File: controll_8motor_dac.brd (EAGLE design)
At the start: 101.6 x 73.3 mm, 60 parts

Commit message: version1 できた． なかなか配線がやばいものだなぁ．
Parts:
- DC-JACK: device con-jack:SPC4077 -> BD6211F:SPC4077
- moved DC-JACK 81.3 mm to (14.0, 20.3)
- moved C1 27.0 mm to (80.0, 49.5), turned to 90 degrees
- moved LTC1660_2 16.3 mm to (62.2, 47.0), turned to 180 degrees
- moved LTC1660_1 10.2 mm to (29.2, 48.3)
- moved CHIPSELECT 7.62 mm to (87.6, 22.9)
- moved MCP3208‐1 7.62 mm to (45.7, 27.9)
- moved ARDUINO11~1 7.62 mm to (92.7, 31.8)
- moved ARDUINO11~13 7.62 mm to (87.6, 31.8)
- moved ARDUINO-5V/GND 5.08 mm to (92.7, 48.3)
- moved C2 3.59 mm to (7.62, 48.3)
- moved 安定化電源1 2.54 mm to (92.7, 57.1)
- moved ARDUINO5V/GND 2.54 mm to (90.2, 48.3)
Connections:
- new net N$26: LTC1660_1.14, M-DRIVER_3.5
- net N$3: no longer LTC1660_1.14, M-DRIVER_3.5
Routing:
- net P-DIORD1: track 0.00 -> 536.0 mm
- net N$97: track 0.00 -> 207.2 mm
- net N$33: track 0.00 -> 196.1 mm
- net ARDUINO-5V/GND: track 0.00 -> 193.9 mm
- net N$39: track 0.00 -> 100.8 mm
- net N$25: track 0.00 -> 90.9 mm
- net N$38: track 0.00 -> 85.5 mm
- net N$59: track 0.00 -> 76.2 mm
- net N$41: track 0.00 -> 69.3 mm
- net N$5: track 0.00 -> 60.1 mm
- net N$42: track 0.00 -> 49.7 mm
- net N$44: track 0.00 -> 44.9 mm
- net N$53: track 0.00 -> 44.6 mm
- net N$56: track 0.00 -> 39.8 mm
- net N$6: track 0.00 -> 37.6 mm
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- added copper zone on layer 1, net GND

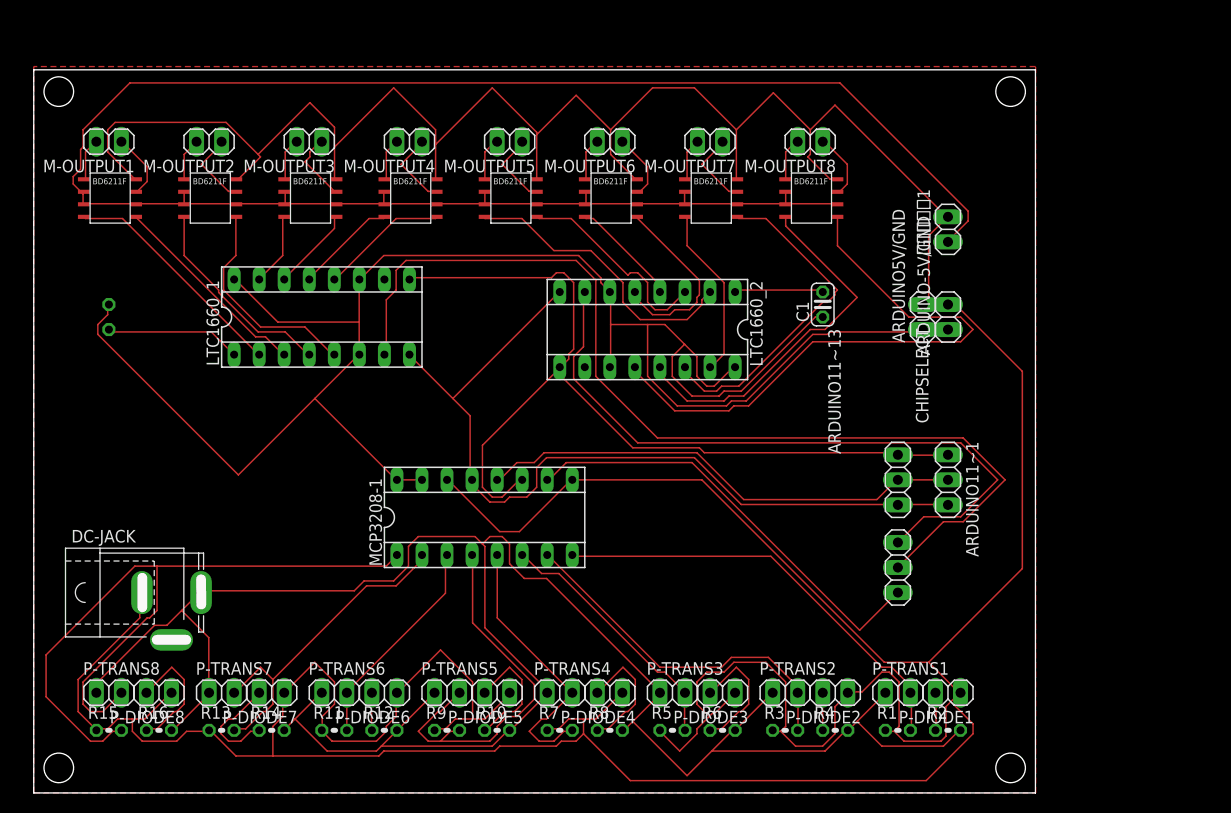
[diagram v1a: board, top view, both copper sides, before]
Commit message: BD6211F-E2 の大きさを変更
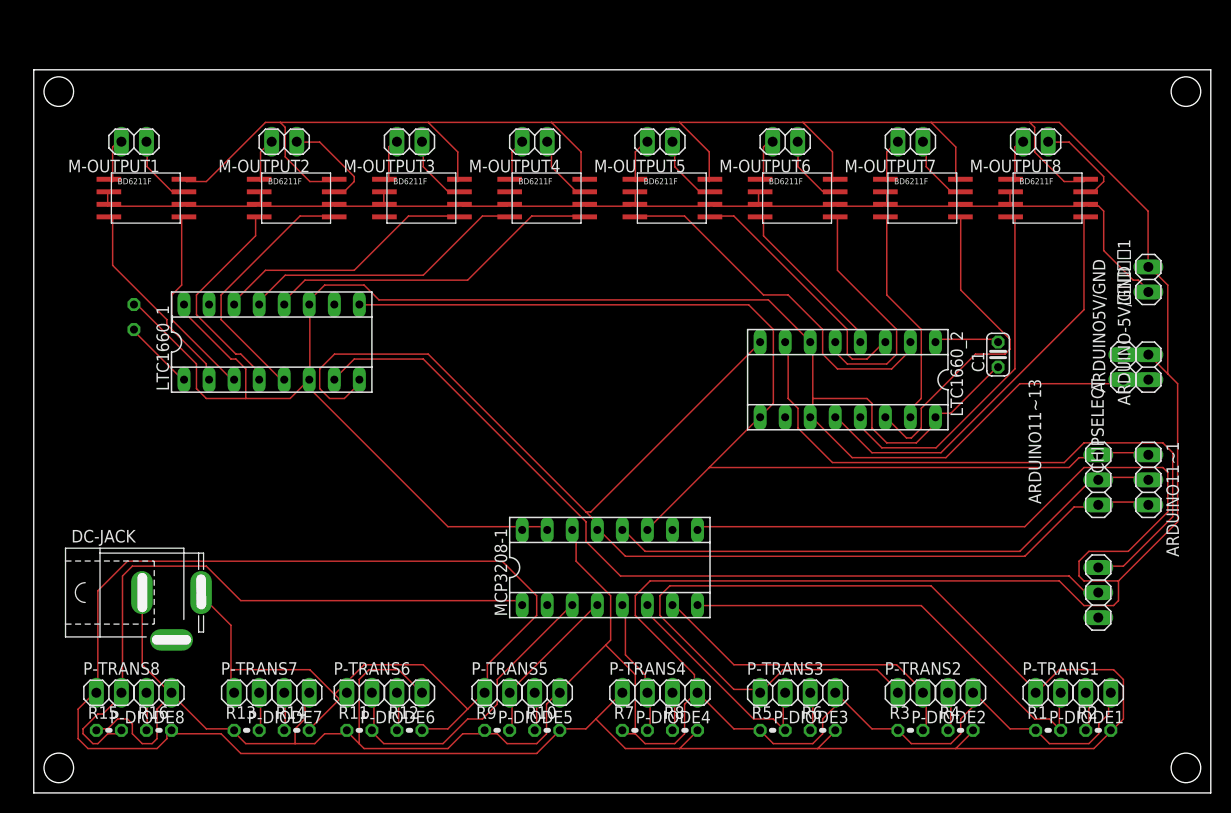
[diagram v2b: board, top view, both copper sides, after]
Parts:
- moved M-DRIVER_8 22.9 mm to (101.6, 59.7)
- moved M-OUTPUT8 22.9 mm to (101.6, 66.0)
- moved ARDUINO-5V/GND 20.9 mm to (113.0, 43.2)
- moved 安定化電源1 20.9 mm to (113.0, 52.1)
- moved LTC1660_2 20.9 mm to (82.5, 41.9)
- moved ARDUINO5V/GND 20.9 mm to (110.5, 43.2)
- moved CHIPSELECT 20.5 mm to (108.0, 20.3)
- moved ARDUINO11~1 20.3 mm to (113.0, 31.8)
- moved ARDUINO11~13 20.3 mm to (108.0, 31.8)
- moved M-DRIVER_7 20.3 mm to (88.9, 59.7)
- moved M-OUTPUT7 20.3 mm to (88.9, 66.0)
- moved C1 18.5 mm to (97.8, 44.5)
- moved M-DRIVER_6 17.8 mm to (76.2, 59.7)
- moved M-OUTPUT6 17.8 mm to (76.2, 66.0)
- moved P-DIODE1 15.2 mm to (108.0, 10.2)
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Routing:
- net N$97: track 207.2 -> 342.7 mm
- net N$33: track 196.1 -> 127.1 mm
- net N$44: track 44.9 -> 0.00 mm
- net N$38: track 85.5 -> 128.7 mm
- net N$58: track 33.7 -> 3.92 mm
- net N$56: track 39.8 -> 16.7 mm
- net N$25: track 90.9 -> 114.0 mm
- net N$1: track 13.1 -> 34.4 mm
- net N$3: track 10.4 -> 29.3 mm
- net N$26: track 8.54 -> 26.7 mm
- net N$5: track 60.1 -> 42.4 mm
- net N$55: track 28.4 -> 14.2 mm
- net N$39: track 100.8 -> 89.3 mm
- net N$59: track 76.2 -> 65.7 mm
- net N$57: track 22.0 -> 32.2 mm
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- removed copper zone on layer 1, net GND
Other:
- board size 101.6 x 73.3 mm -> 119.4 x 73.3 mm

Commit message: 竹内君が配線してくれたバージョン．回路図は変わってない 100 % になってるよ！ DCジャックの向きが逆
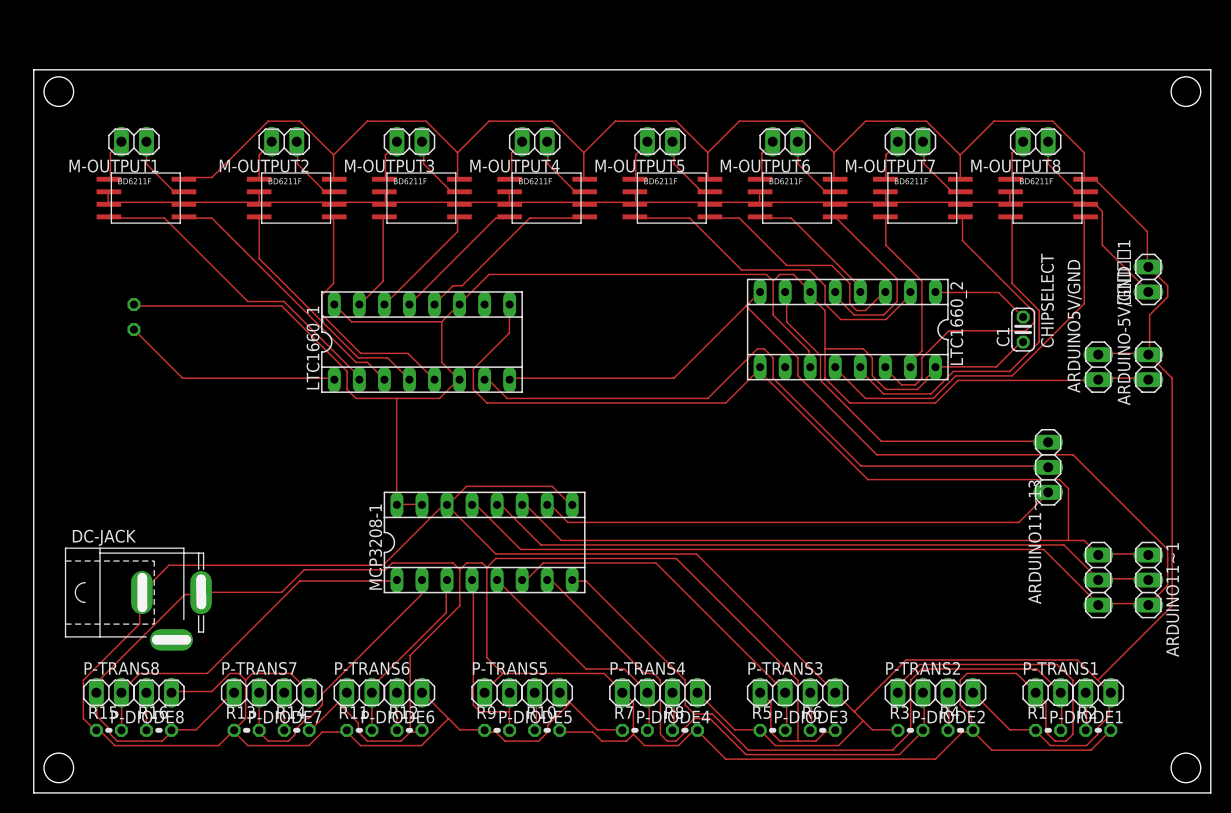
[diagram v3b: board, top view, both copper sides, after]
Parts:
- moved LTC1660_1 15.2 mm to (39.4, 45.7)
- moved CHIPSELECT 13.7 mm to (102.9, 33.0)
- moved MCP3208‐1 13.0 mm to (45.7, 25.4)
- moved ARDUINO11~1 10.2 mm to (113.0, 21.6)
- moved ARDUINO11~13 10.2 mm to (108.0, 21.6)
- moved LTC1660_2 5.08 mm to (82.5, 47.0)
- moved C1 3.59 mm to (100.3, 47.0)
- moved ARDUINO5V/GND 2.54 mm to (108.0, 43.2)
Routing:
- net P-DIORD1: track 541.9 -> 475.1 mm
- net N$44: track 0.00 -> 52.9 mm
- net N$97: track 342.7 -> 297.9 mm
- net N$25: track 114.0 -> 149.0 mm
- net N$38: track 128.7 -> 162.5 mm
- net N$41: track 66.2 -> 36.2 mm
- net N$59: track 65.7 -> 36.6 mm
- net N$58: track 3.92 -> 29.4 mm
- net N$53: track 45.8 -> 69.6 mm
- net N$39: track 89.3 -> 66.3 mm
- net N$52: track 33.4 -> 55.8 mm
- net N$1: track 34.4 -> 18.9 mm
- net N$3: track 29.3 -> 13.9 mm
- net N$34: track 7.22 -> 22.5 mm
- net N$26: track 26.7 -> 12.1 mm
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
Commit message: DCジャックを長穴＆外向きにした
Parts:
- removed DC-JACK: (no value), BD6211F:SPC4077
- added U$1: 2.1MMJACKTHM, adafruit:PJ-102A
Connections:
- net N$97: now also U$1.TIP; no longer DC-JACK.3
- net P-DIORD1: now also U$1.RING; no longer DC-JACK.1
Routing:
- net P-DIORD1: track 475.1 -> 492.6 mm
- net N$97: track 297.9 -> 302.7 mm

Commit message: 基板加工機の使い方を間違えていたことに気づいたので DCジャックのつなぎ方を戻した． さらに，このまま掘ってしまうと表面実装がミラーになってしまうのでこれから 修正する
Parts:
- added DC-JUMP: (no value), pinhead:1X02
- moved U$1 2.54 mm to (7.62, 27.9), flipped to the top, turned to 90 degrees
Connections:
- net N$97: now also DC-JUMP.1
- net P-DIORD1: now also DC-JUMP.2
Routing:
- net N$97: track 302.7 -> 309.4 mm
- net P-DIORD1: track 492.6 -> 491.9 mm
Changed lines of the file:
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@@
 <element name="M-DRIVER_6" library="BD6211F" package="BD6211F-E2" value="BD6211F-E2" x="76.2" y="59.69" smashed="yes"/>
 <element name="M-DRIVER_5" library="BD6211F" package="BD6211F-E2" value="BD6211F-E2" x="63.5" y="59.69" smashed="yes"/>
-<element name="U$1" library="adafruit" package="PJ-102A" value="2.1MMJACKTHM" x="7.62" y="25.4" smashed="yes" rot="MR270"/>
+<element name="U$1" library="adafruit" package="PJ-102A" value="2.1MMJACKTHM" x="7.62" y="27.94" smashed="yes" rot="R90"/>
+<element name="DC-JUMP" library="pinhead" library_urn="urn:adsk.eagle:library:325" package="1X02" package3d_urn="urn:adsk.eagle:package:22435/2" value="" x="27.94" y="27.94" smashed="yes" rot="R90">
+<attribute name="NAME" x="26.1112" y="25.3238" size="1.27" layer="25" ratio="10" rot="R90"/>
+<attribute name="POPULARITY" value="98" x="27.94" y="27.94" size="1.778" layer="27" rot="R90" display="off"/>
+<attribute name="VALUE" x="31.115" y="25.4" size="1.27" layer="27" rot="R90"/>
+</element>
 </elements>
 <signals>
@@
 <wire x1="43.2054" y1="22.6314" x2="42.5196" y2="23.3172" width="0.1524" layer="1"/>
 <contactref element="U$1" pad="TIP"/>
-<wire x1="35.6616" y1="22.6314" x2="19.5786" y2="22.6314" width="0.1524" layer="1"/>
+<wire x1="35.6616" y1="22.6314" x2="27.94" y2="22.6314" width="0.1524" layer="1"/>
+<wire x1="27.94" y1="22.6314" x2="19.5786" y2="22.6314" width="0.1524" layer="1"/>
 <wire x1="6.63855" y1="10.287" x2="6.4008" y2="10.287" width="0.1524" layer="1"/>
-<wire x1="19.5786" y1="22.6314" x2="16.91" y2="25.3" width="0.1524" layer="1"/>
 <wire x1="7.1072" y1="10.16" x2="6.35" y2="10.16" width="0.1524" layer="1"/>
 <wire x1="19.5786" y1="22.6314" x2="9.0122" y2="12.065" width="0.1524" layer="1"/>
@@
 <wire x1="7.747" y1="11.39545" x2="7.747" y2="10.7998" width="0.1524" layer="1"/>
 <wire x1="7.747" y1="10.7998" x2="7.1072" y2="10.16" width="0.1524" layer="1"/>
+<wire x1="19.5786" y1="22.8314" x2="16.91" y2="25.5" width="0.1524" layer="1"/>
+<wire x1="16.91" y1="28.04" x2="16.91" y2="25.5" width="0.1524" layer="1"/>
+<wire x1="19.5786" y1="22.8314" x2="19.5786" y2="22.6314" width="0.1524" layer="1"/>
+<contactref element="DC-JUMP" pad="1"/>
+<wire x1="27.94" y1="26.67" x2="27.94" y2="22.6314" width="0.1524" layer="1"/>
 </signal>
 <signal name="ARDUINO-5V/GND">
@@
 <wire x1="21.4884" y1="11.43" x2="22.1742" y2="12.1158" width="0.1524" layer="1"/>
 <wire x1="27.8892" y1="10.287" x2="27.94" y2="10.16" width="0.1524" layer="1"/>
-<wire x1="10.7442" y1="17.145" x2="5.0292" y2="11.43" width="0.1524" layer="1"/>
-<wire x1="5.0292" y1="7.5438" x2="5.0292" y2="11.43" width="0.1524" layer="1"/>
+<wire x1="5.0292" y1="11.43" x2="5.0292" y2="7.5438" width="0.1524" layer="1"/>
 <wire x1="6.1722" y1="6.4008" x2="5.0292" y2="7.5438" width="0.1524" layer="1"/>
 <wire x1="6.1722" y1="6.4008" x2="6.35" y2="6.35" width="0.1524" layer="1"/>
-<wire x1="41.3766" y1="29.0322" x2="41.8338" y2="29.0322" width="0.1524" layer="1"/>
-<wire x1="41.3766" y1="29.0322" x2="35.433" y2="23.0886" width="0.1524" layer="1"/>
-<wire x1="41.8338" y1="29.0322" x2="41.91" y2="29.21" width="0.1524" layer="1"/>
+<wire x1="36.2966" y1="26.4922" x2="41.8338" y2="26.4922" width="0.1524" layer="1"/>
+<wire x1="41.91" y1="26.67" x2="41.91" y2="29.21" width="0.1524" layer="1"/>
+<wire x1="41.91" y1="26.67" x2="41.8338" y2="26.4922" width="0.1524" layer="1"/>
 <wire x1="39.3192" y1="4.8006" x2="42.0624" y2="7.5438" width="0.1524" layer="1"/>
 <wire x1="33.147" y1="4.8006" x2="39.3192" y2="4.8006" width="0.1524" layer="1"/>
@@
 <wire x1="42.0624" y1="29.0322" x2="41.91" y2="29.21" width="0.1524" layer="1"/>
 <contactref element="U$1" pad="RING"/>
-<wire x1="12.89706875" y1="25.3" x2="12.848534375" y2="25.251465625" width="0.1524" layer="1"/>
-<wire x1="12.848534375" y1="25.251465625" x2="12.75806875" y2="25.161" width="0.1524" layer="1"/>
-<wire x1="35.433" y1="23.0886" x2="22.6314" y2="23.0886" width="0.1524" layer="1"/>
-<wire x1="22.6314" y1="23.0886" x2="19.691" y2="26.029" width="0.1524" layer="1"/>
-<wire x1="19.691" y1="26.029" x2="19.691" y2="28.15193125" width="0.1524" layer="1"/>
-<wire x1="19.691" y1="28.15193125" x2="15.06193125" y2="32.781" width="0.1524" layer="1"/>
-<wire x1="12.75806875" y1="32.781" x2="11.01" y2="31.03293125" width="0.1524" layer="1"/>
-<wire x1="11.01" y1="31.03293125" x2="11.01" y2="25.3" width="0.1524" layer="1"/>
-<wire x1="15.06193125" y1="32.781" x2="12.75806875" y2="32.781" width="0.1524" layer="1"/>
-<wire x1="11.01" y1="25.3" x2="10.7442" y2="25.0342" width="0.1524" layer="1"/>
-<wire x1="10.7442" y1="25.0342" x2="10.7442" y2="17.145" width="0.1524" layer="1"/>
-<wire x1="11.01" y1="25.3" x2="12.8" y2="25.3" width="0.1524" layer="1"/>
-<wire x1="12.8" y1="25.3" x2="12.848534375" y2="25.251465625" width="0.1524" layer="1"/>
+<wire x1="36.2966" y1="26.4922" x2="30.0078" y2="32.781" width="0.1524" layer="1"/>
+<wire x1="12.75806875" y1="32.781" x2="10.7442" y2="30.76713125" width="0.1524" layer="1"/>
+<wire x1="30.0078" y1="32.781" x2="27.94" y2="32.781" width="0.1524" layer="1"/>
+<wire x1="27.94" y1="32.781" x2="12.75806875" y2="32.781" width="0.1524" layer="1"/>
+<wire x1="11.01" y1="28.04" x2="11.01" y2="27.94" width="0.1524" layer="1"/>
+<wire x1="11.01" y1="27.94" x2="11.01" y2="17.4108" width="0.1524" layer="1"/>
+<wire x1="11.01" y1="17.4108" x2="5.0292" y2="11.43" width="0.1524" layer="1"/>
+<wire x1="10.7442" y1="30.76713125" x2="10.7442" y2="28.2058" width="0.1524" layer="1"/>
+<wire x1="10.7442" y1="28.2058" x2="11.01" y2="27.94" width="0.1524" layer="1"/>
+<contactref element="DC-JUMP" pad="2"/>
+<wire x1="27.94" y1="29.21" x2="27.94" y2="32.781" width="0.1524" layer="1"/>
 </signal>
 <signal name="N$33">
